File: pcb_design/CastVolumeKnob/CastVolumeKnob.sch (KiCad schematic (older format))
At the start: 1 part

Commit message: KiCad schematic changes
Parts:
- added D?: WS2812, LED_SMD:LED_WS2812_PLCC6_5.0x5.0mm_P1.6mm, symbol LED:WS2812
- added Q?: 2N3904, Package_TO_SOT_THT:TO-92_Inline, symbol Transistor_BJT:2N3904
- added Q?: IRF9540N, Package_TO_SOT_THT:TO-220-3_Vertical, symbol Transistor_FET:IRF9540N
- added Q?: 2N7000, Package_TO_SOT_THT:TO-92_Inline, symbol Transistor_FET:2N7000
- added R?: R, symbol Device:R
- added SW?: Rotary_Encoder_Switch, symbol Device:Rotary_Encoder_Switch
- added U?: ATtiny85-20PU, Package_DIP:DIP-8_W7.62mm, symbol MCU_Microchip_ATtiny:ATtiny85-20PU
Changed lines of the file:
@@
 EESchema Schematic File Version 4
+LIBS:CastVolumeKnob-cache
 EELAYER 26 0
 EELAYER END
@@
 	1    0    0    -1
 $EndComp
+$Comp
+L Device:Rotary_Encoder_Switch SW?
+U 1 1 5BE6F48A
+P 7950 1850
+F 0 "SW?" H 7950 2217 50  0000 C CNN
+F 1 "Rotary_Encoder_Switch" H 7950 2126 50  0000 C CNN
+F 2 "" H 7800 2010 50  0001 C CNN
+F 3 "~" H 7950 2110 50  0001 C CNN
+	1    7950 1850
+	1    0    0    -1
+$EndComp
+$Comp
+L MCU_Microchip_ATtiny:ATtiny85-20PU U?
+U 1 1 5BE6F59F
+P 3050 1850
+F 0 "U?" H 2520 1896 50  0000 R CNN
+F 1 "ATtiny85-20PU" H 2520 1805 50  0000 R CNN
+F 2 "Package_DIP:DIP-8_W7.62mm" H 3050 1850 50  0001 C CIN
+F 3 "http://ww1.microchip.com/downloads/en/DeviceDoc/atmel-2586-avr-8-bit-microcontroller-attiny25-attiny45-attiny85_datasheet.pdf" H 3050 1850 50  0001 C CNN
+	1    3050 1850
+	1    0    0    -1
+$EndComp
+$Comp
+L LED:WS2812 D?
+U 1 1 5BE6F679
+P 8050 4000
+F 0 "D?" H 8391 4046 50  0000 L CNN
+F 1 "WS2812" H 8391 3955 50  0000 L CNN
+F 2 "LED_SMD:LED_WS2812_PLCC6_5.0x5.0mm_P1.6mm" H 8100 3700 50  0001 L TNN
+F 3 "https://cdn-shop.adafruit.com/datasheets/WS2812.pdf" H 8150 3625 50  0001 L TNN
+	1    8050 4000
+	1    0    0    -1
+$EndComp
+$Comp
+L Transistor_BJT:2N3904 Q?
+U 1 1 5BE6F760
+P 6450 4700
+F 0 "Q?" H 6641 4746 50  0000 L CNN
+F 1 "2N3904" H 6641 4655 50  0000 L CNN
+F 2 "Package_TO_SOT_THT:TO-92_Inline" H 6650 4625 50  0001 L CIN
+F 3 "https://www.fairchildsemi.com/datasheets/2N/2N3904.pdf" H 6450 4700 50  0001 L CNN
+	1    6450 4700
+	1    0    0    -1
+$EndComp
+$Comp
+L Transistor_FET:IRF9540N Q?
+U 1 1 5BE6F824
+P 5250 5400
+F 0 "Q?" H 5455 5446 50  0000 L CNN
+F 1 "IRF9540N" H 5455 5355 50  0000 L CNN
+F 2 "Package_TO_SOT_THT:TO-220-3_Vertical" H 5450 5325 50  0001 L CIN
+F 3 "http://www.irf.com/product-info/datasheets/data/irf9540n.pdf" H 5250 5400 50  0001 L CNN
+	1    5250 5400
+	1    0    0    -1
+$EndComp
+$Comp
+L Device:R R?
+U 1 1 5BE6F887
+P 5500 4850
+F 0 "R?" H 5570 4896 50  0000 L CNN
+F 1 "R" H 5570 4805 50  0000 L CNN
+F 2 "" V 5430 4850 50  0001 C CNN
+F 3 "~" H 5500 4850 50  0001 C CNN
+	1    5500 4850
+	1    0    0    -1
+$EndComp
+$Comp
+L Transistor_FET:2N7000 Q?
+U 1 1 5BE6F980
+P 9900 1950
+F 0 "Q?" H 10105 1996 50  0000 L CNN
+F 1 "2N7000" H 10105 1905 50  0000 L CNN
+F 2 "Package_TO_SOT_THT:TO-92_Inline" H 10100 1875 50  0001 L CIN
+F 3 "https://www.fairchildsemi.com/datasheets/2N/2N7000.pdf" H 9900 1950 50  0001 L CNN
+	1    9900 1950
+	1    0    0    -1
+$EndComp

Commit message: Kicad on linux
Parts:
- U?: symbol wemos_mini:WeMos_mini -> CastVolumeKnob-rescue:WeMos_mini-wemos_mini
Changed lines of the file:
@@
 $EndDescr
 $Comp
-L wemos_mini:WeMos_mini U?
+L CastVolumeKnob-rescue:WeMos_mini-wemos_mini U?
 U 1 1 5BE35DA7
 P 5250 3600

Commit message: Improved schematics
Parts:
- removed SW?: Rotary_Encoder_Switch, symbol Device:Rotary_Encoder_Switch
- added E?: KY-040, symbol KY-040:KY-040
- added R?: 1K, symbol Device:R
- added R? (x2): 10K, symbol Device:R
- added SW?: SW_SPST, symbol Switch:SW_SPST
- R?: value R -> 10K
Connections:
- net labels added: +3.3V, +5V, GND, LED_RING, LED_V, NEO_PIXEL, SWITCH, WAKE_PIN
- wire segments 0 -> 53
- no-connect marks 0 -> 2
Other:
- moved on the sheet: Q?, R?, U?

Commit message: schematic fixes
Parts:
- removed D?: WS2812, LED_SMD:LED_WS2812_PLCC6_5.0x5.0mm_P1.6mm, symbol LED:WS2812
- removed E?: KY-040, symbol KY-040:KY-040
- added J?: NeoPixelRing, symbol Connector_Generic:Conn_01x03
- added J? (x2): Conn_01x08, symbol Connector_Generic:Conn_01x08
- added J?: Encoder, symbol Connector_Generic:Conn_01x05
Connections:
- net labels added: CAST_SW, E_CLK, E_DT
- net labels removed: LED_V
- wire segments 53 -> 105
- no-connect marks 2 -> 0
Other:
- moved on the sheet: Q?, R?, SW?, U?

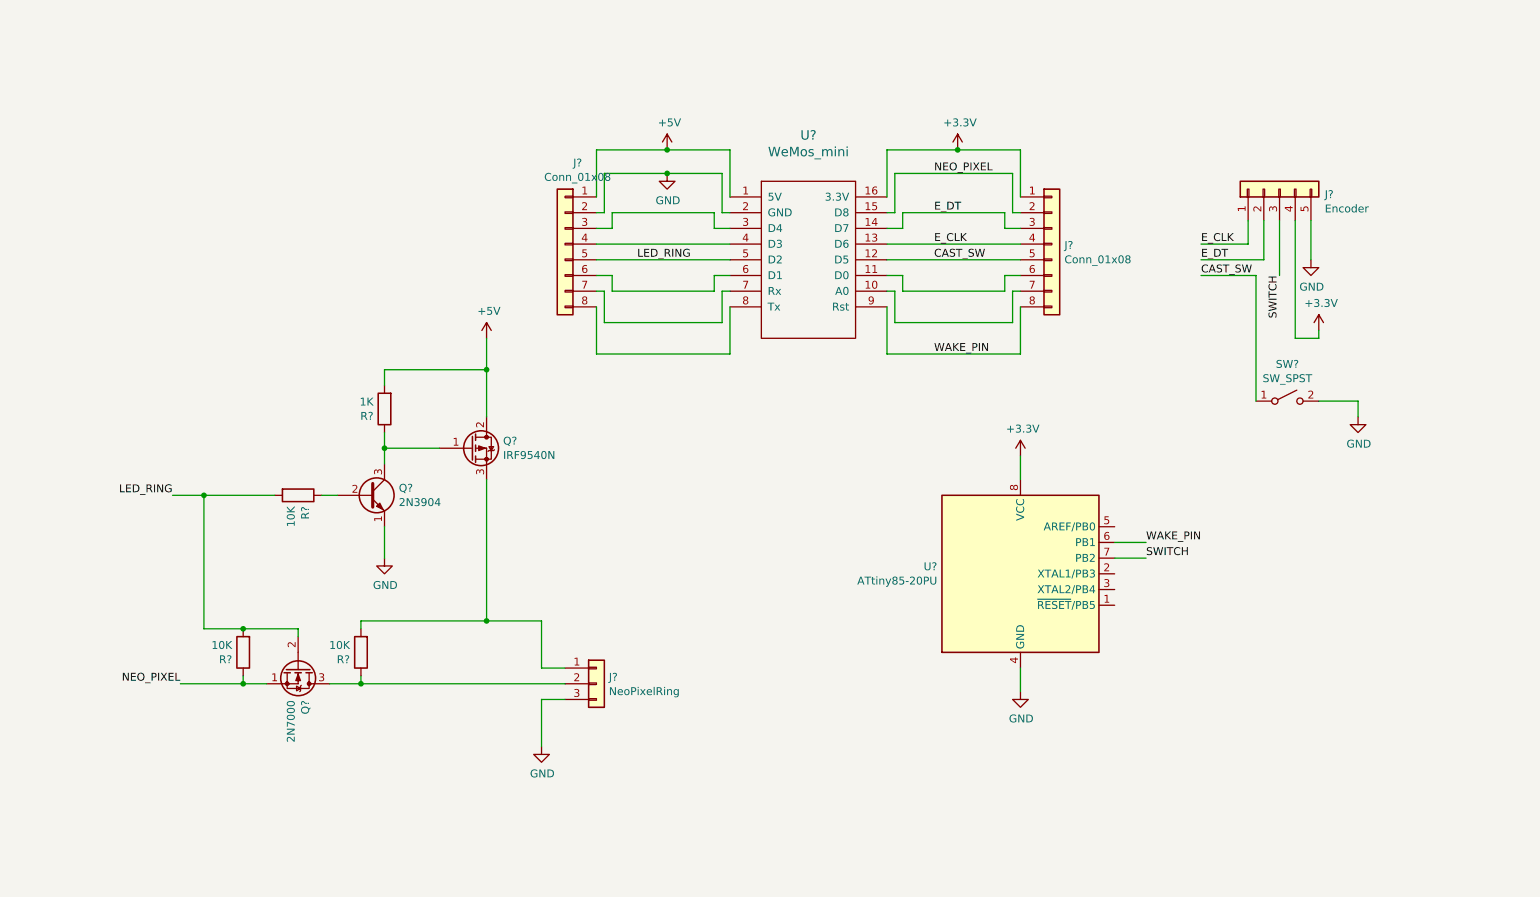
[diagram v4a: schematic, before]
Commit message: PCB schematic changes
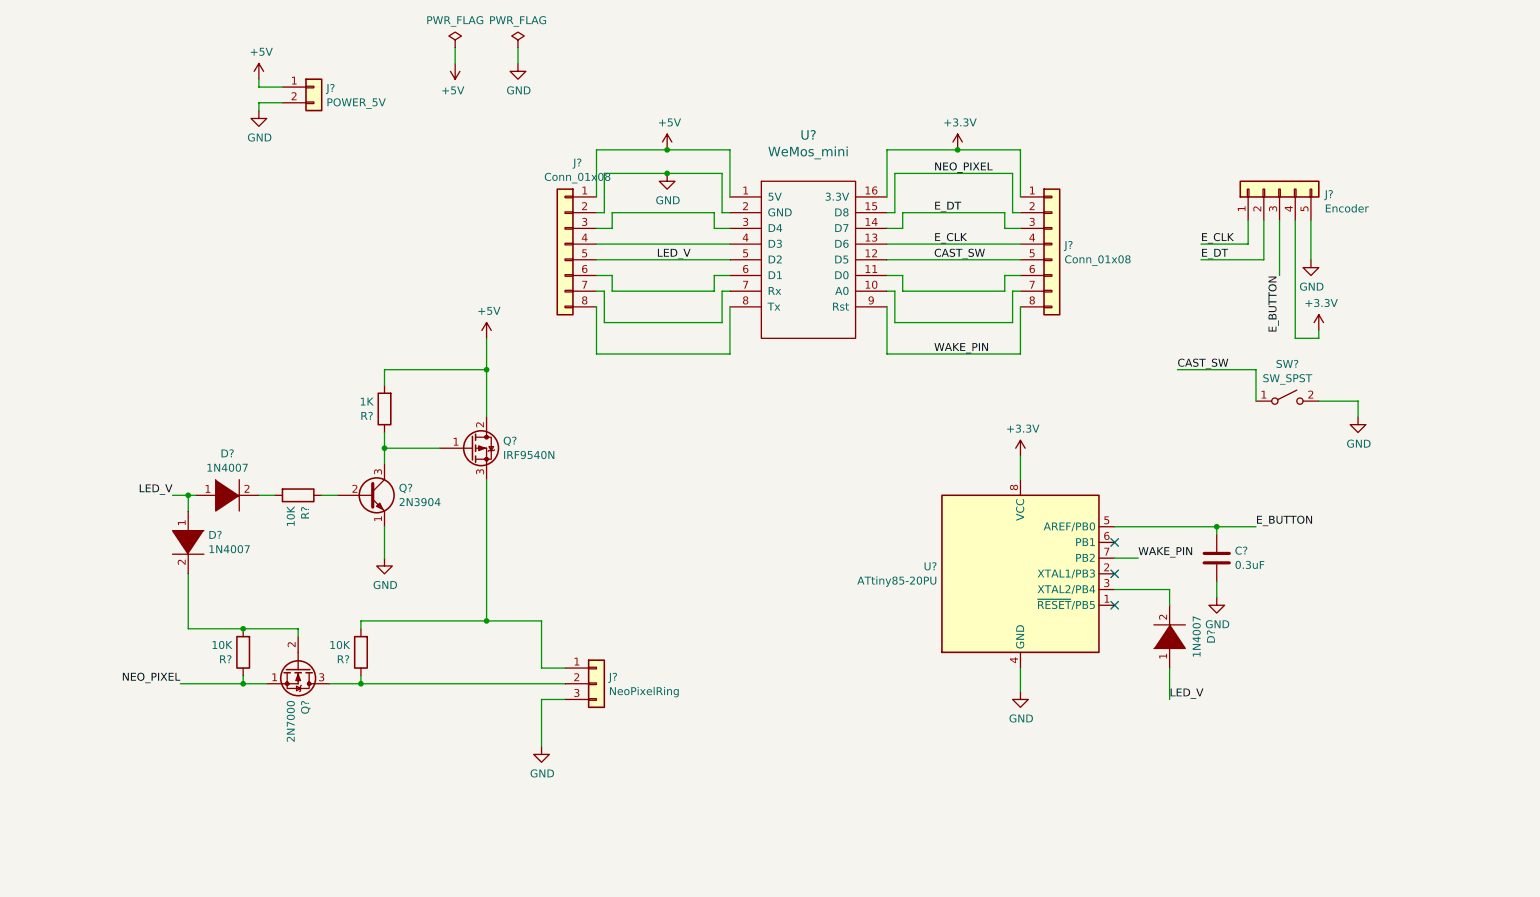
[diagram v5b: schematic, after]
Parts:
- added C?: 0.3uF, symbol Device:C
- added D? (x3): 1N4007, symbol pspice:DIODE
- added J?: POWER_5V, symbol Connector_Generic:Conn_01x02
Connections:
- net +5V: now also J?.1 (Pin_1)
- net GND: now also C?.2, J?.2 (Pin_2)
- net WAKE_PIN: now also U?.7 (PB2); no longer U?.6 (PB1)
- net at U?.3 (XTAL2/PB4): now also D?.2 (A)
- net E_BUTTON: now reaches U?.5 (AREF/PB0)
- net E_BUTTON: now also J?.3 (Pin_3), C?.1
- removed net LED_RING: J?.5 (Pin_5), Q?.2 (G), R?.2, R?.2, U?.5 (D2)
- removed net SWITCH: J?.3 (Pin_3), U?.7 (PB2)
- new net: D?.2 (A), R?.2
- new net: D?.2 (A), Q?.2 (G), R?.2
- new net LED_V: D?.1 (K), D?.1 (K), D?.1 (K), J?.5 (Pin_5), U?.5 (D2)
- no-connect marks 0 -> 3
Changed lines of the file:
@@
 $EndComp
 Text Label 5100 2400 2    50   ~ 0
-LED_RING
+LED_V
 Text Label 1800 3900 2    50   ~ 0
-LED_RING
+LED_V
 Wire Wire Line
 	2250 5100 1850 5100
@@
 $EndComp
 Wire Wire Line
-	8700 3300 8700 2500
+	8700 3300 8700 3100
 Wire Wire Line
 	8950 2900 9100 2900
@@
 Wire Wire Line
 	7200 5000 7200 5150
-Text Label 8000 4200 0    50   ~ 0
+Text Label 7950 4300 0    50   ~ 0
 WAKE_PIN
 Text Label 6650 3000 0    50   ~ 0
 WAKE_PIN
-Wire Wire Line
-	8000 4200 7800 4200
 Text Label 8850 2500 3    50   ~ 0
-SWITCH
-Text Label 8000 4300 0    50   ~ 0
-SWITCH
-Wire Wire Line
-	8000 4300 7800 4300
+E_BUTTON
+Text Label 8700 4100 0    50   ~ 0
+E_BUTTON
 $Comp
 L Connector_Generic:Conn_01x03 J?
@@
 Connection ~ 2250 4750
 Wire Wire Line
-	1800 3900 2000 3900
-Wire Wire Line
-	2000 4750 2000 3900
-Wire Wire Line
-	2000 4750 2250 4750
-Connection ~ 2000 3900
-Wire Wire Line
-	2000 3900 2450 3900
-Wire Wire Line
 	4500 2000 4500 1700
 Wire Wire Line
@@
 Text Label 8350 2400 0    50   ~ 0
 E_DT
-Text Label 8350 2500 0    50   ~ 0
+Text Label 8200 3100 0    50   ~ 0
 CAST_SW
 Wire Wire Line
@@
 Wire Wire Line
 	8750 2400 8350 2400
-Wire Wire Line
-	8350 2500 8700 2500
 Text Label 6650 2300 0    50   ~ 0
 E_CLK
@@
 Wire Wire Line
 	9050 2150 9050 2400
+$Comp
+L pspice:DIODE D?
+U 1 1 5BF83B53
+P 1900 4200
+F 0 "D?" V 1854 4328 50  0000 L CNN
+F 1 "1N4007" V 1945 4328 50  0000 L CNN
+F 2 "" H 1900 4200 50  0001 C CNN
+F 3 "~" H 1900 4200 50  0001 C CNN
+	1    1900 4200
+	0    1    1    0
+$EndComp
+$Comp
+L pspice:DIODE D?
+U 1 1 5BF83C8F
+P 2150 3900
+F 0 "D?" H 2150 4165 50  0000 C CNN
+F 1 "1N4007" H 2150 4074 50  0000 C CNN
+F 2 "" H 2150 3900 50  0001 C CNN
+F 3 "~" H 2150 3900 50  0001 C CNN
+	1    2150 3900
+	1    0    0    -1
+$EndComp
+$Comp
+L pspice:DIODE D?
+U 1 1 5BF83D37
+P 8150 4800
+F 0 "D?" H 8150 4535 50  0000 C CNN
+F 1 "1N4007" H 8150 4626 50  0000 C CNN
+F 2 "" H 8150 4800 50  0001 C CNN
+F 3 "~" H 8150 4800 50  0001 C CNN
+	1    8150 4800
+	0    -1   -1   0
+$EndComp
+Text Label 8150 5200 0    50   ~ 0
+LED_V
+Wire Wire Line
+	1800 3900 1900 3900
+Wire Wire Line
+	2350 3900 2450 3900
+Wire Wire Line
+	1900 4000 1900 3900
+Connection ~ 1900 3900
+Wire Wire Line
+	1900 3900 1950 3900
+Wire Wire Line
+	1900 4750 2250 4750
+Wire Wire Line
+	1900 4400 1900 4750
+$Comp
+L Device:C C?
+U 1 1 5BF99E77
+P 8450 4300
+F 0 "C?" H 8565 4346 50  0000 L CNN
+F 1 "0.3uF" H 8565 4255 50  0000 L CNN
+F 2 "" H 8488 4150 50  0001 C CNN
+F 3 "~" H 8450 4300 50  0001 C CNN
+	1    8450 4300
+	1    0    0    -1
+$EndComp
+Wire Wire Line
+	8450 4100 8450 4150
+Wire Wire Line
+	8450 4100 8700 4100
+$Comp
+L power:GND #PWR?
+U 1 1 5BFA2B6D
+P 8450 4550
+F 0 "#PWR?" H 8450 4300 50  0001 C CNN
+F 1 "GND" H 8455 4377 50  0000 C CNN
+F 2 "" H 8450 4550 50  0001 C CNN
+F 3 "" H 8450 4550 50  0001 C CNN
+	1    8450 4550
+	1    0    0    -1
+$EndComp
+Wire Wire Line
+	8150 5000 8150 5200
+Wire Wire Line
+	8450 4450 8450 4550
+Wire Wire Line
+	8200 3100 8700 3100
+$Comp
+L Connector_Generic:Conn_01x02 J?
+U 1 1 5BF858A4
+P 2700 1300
+F 0 "J?" H 2780 1292 50  0000 L CNN
+F 1 "POWER_5V" H 2780 1201 50  0000 L CNN
+F 2 "" H 2700 1300 50  0001 C CNN
+F 3 "~" H 2700 1300 50  0001 C CNN
+	1    2700 1300
+	1    0    0    -1
+$EndComp
+$Comp
+L power:+5V #PWR?
+U 1 1 5BF85A88
+P 2350 1250
+F 0 "#PWR?" H 2350 1100 50  0001 C CNN
+F 1 "+5V" H 2365 1423 50  0000 C CNN
+F 2 "" H 2350 1250 50  0001 C CNN
+F 3 "" H 2350 1250 50  0001 C CNN
+	1    2350 1250
+	1    0    0    -1
+$EndComp
+$Comp
+L power:GND #PWR?
+U 1 1 5BF85AB9
+P 2350 1450
+F 0 "#PWR?" H 2350 1200 50  0001 C CNN
+F 1 "GND" H 2355 1277 50  0000 C CNN
+F 2 "" H 2350 1450 50  0001 C CNN
+F 3 "" H 2350 1450 50  0001 C CNN
+	1    2350 1450
+	1    0    0    -1
+$EndComp
+Wire Wire Line
+	2500 1300 2350 1300
+Wire Wire Line
+	2350 1300 2350 1250
+Wire Wire Line
+	2500 1400 2350 1400
+Wire Wire Line
+	2350 1400 2350 1450
+Wire Wire Line
+	7800 4100 8450 4100
+Connection ~ 8450 4100
+Wire Wire Line
+	7800 4500 8150 4500
+Wire Wire Line
+	8150 4500 8150 4600
+Wire Wire Line
+	7800 4300 7950 4300
+NoConn ~ 7800 4200
+NoConn ~ 7800 4400
+NoConn ~ 7800 4600
+$Comp
+L power:PWR_FLAG #FLG?
+U 1 1 5BFCA3FA
+P 3600 1050
+F 0 "#FLG?" H 3600 1125 50  0001 C CNN
+F 1 "PWR_FLAG" H 3600 1224 50  0000 C CNN
+F 2 "" H 3600 1050 50  0001 C CNN
+F 3 "~" H 3600 1050 50  0001 C CNN
+	1    3600 1050
+	1    0    0    -1
+$EndComp
+$Comp
+L power:PWR_FLAG #FLG?
+U 1 1 5BFCA49C
+P 4000 1050
+F 0 "#FLG?" H 4000 1125 50  0001 C CNN
+F 1 "PWR_FLAG" H 4000 1224 50  0000 C CNN
+F 2 "" H 4000 1050 50  0001 C CNN
+F 3 "~" H 4000 1050 50  0001 C CNN
+	1    4000 1050
+	1    0    0    -1
+$EndComp
+$Comp
+L power:GND #PWR?
+U 1 1 5BFCA524
+P 4000 1150
+F 0 "#PWR?" H 4000 900 50  0001 C CNN
+F 1 "GND" H 4005 977 50  0000 C CNN
+F 2 "" H 4000 1150 50  0001 C CNN
+F 3 "" H 4000 1150 50  0001 C CNN
+	1    4000 1150
+	1    0    0    -1
+$EndComp
+$Comp
+L power:+5V #PWR?
+U 1 1 5BFCA555
+P 3600 1150
+F 0 "#PWR?" H 3600 1000 50  0001 C CNN
+F 1 "+5V" H 3615 1323 50  0000 C CNN
+F 2 "" H 3600 1150 50  0001 C CNN
+F 3 "" H 3600 1150 50  0001 C CNN
+	1    3600 1150
+	-1   0    0    1
+$EndComp
+Wire Wire Line
+	3600 1050 3600 1150
+Wire Wire Line
+	4000 1050 4000 1150
 $EndSCHEMATC

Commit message: PCB v01 - oredered version
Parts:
- removed D? (x3): 1N4007, symbol pspice:DIODE
- removed SW?: SW_SPST, symbol Switch:SW_SPST
- added J6: ATTINY85, Connector_PinHeader_2.54mm:PinHeader_1x06_P2.54mm_Vertical, symbol Connector_Generic:Conn_01x06
- C1: renamed from C?; footprint (none) -> Capacitor_THT:C_Disc_D3.8mm_W2.6mm_P2.50mm
- J1: renamed from J?; footprint (none) -> Connector_PinHeader_2.54mm:PinHeader_1x02_P2.54mm_Horizontal
- J2, J4: renamed from J?; footprint (none) -> Connector_PinHeader_2.54mm:PinHeader_1x08_P2.54mm_Vertical
- J3: renamed from J?; footprint (none) -> Connector_PinHeader_2.54mm:PinHeader_1x03_P2.54mm_Horizontal
- J5: renamed from J?; footprint (none) -> Connector_PinHeader_2.54mm:PinHeader_1x05_P2.54mm_Horizontal
- Q3: renamed from Q?; footprint Package_TO_SOT_THT:TO-220-3_Vertical -> Package_TO_SOT_THT:TO-220-3_Horizontal_TabDown
- R1, R2, R3, R4: renamed from R?; footprint (none) -> Resistor_THT:R_Axial_DIN0207_L6.3mm_D2.5mm_P10.16mm_Horizontal
- U1: renamed from U?; footprint (none) -> wemos-d1-mini:wemos-d1-mini-connectors-only
- U2: renamed from U?; footprint Package_DIP:DIP-8_W7.62mm -> Package_DIP:DIP-8_W7.62mm_Socket_LongPads
- gave numbers to parts that had none: 2
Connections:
- net E_BUTTON: now also J6.1 (Pin_1)
- net LED_V: now also Q1.2 (G), R1.2, R2.2, U2.3 (XTAL2/PB4), J6.5 (Pin_5)
- net WAKE_PIN: now also J6.3 (Pin_3)
- net BUTTON: now reaches J2.6 (Pin_6), U1.6 (D1)
- net BUTTON: now also U2.2 (XTAL1/PB3), J6.4 (Pin_4)
- net at U2.1 (~RESET~/PB5): now also J6.6 (Pin_6)
- net at U2.6 (PB1): now also J6.2 (Pin_2)
- net at Q3.3 (S), R3.2: now also J3.2 (Pin_2); no longer J3.1 (Pin_1)
- net at Q1.3 (D), R3.1: now also J3.1 (Pin_1); no longer J3.2 (Pin_2)
- net CAST_SW: no longer names the net of J4.5 (Pin_5), U1.12 (D5)
- no-connect marks 3 -> 0
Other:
- moved on the sheet: C1

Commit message: Fixed mosfet footprint for v2 pcb
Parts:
- Q3: footprint Package_TO_SOT_THT:TO-220-3_Horizontal_TabDown -> Package-TO:TO-220-3_Horizontal_TabDown-132
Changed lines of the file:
@@
 F 0 "Q3" H 3905 3646 50  0000 L CNN
 F 1 "IRF9540N" H 3905 3555 50  0000 L CNN
-F 2 "Package_TO_SOT_THT:TO-220-3_Horizontal_TabDown" H 3900 3525 50  0001 L CIN
+F 2 "Package-TO:TO-220-3_Horizontal_TabDown-132" H 3900 3525 50  0001 L CIN
 F 3 "" H 3700 3600 50  0001 L CNN
 	1    3700 3600
